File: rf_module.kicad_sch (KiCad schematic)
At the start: 32 parts, among them J10 HJ-SMA405, J9 1042240820, Q1 BC848, Q2 BC848, U4 SIM800C

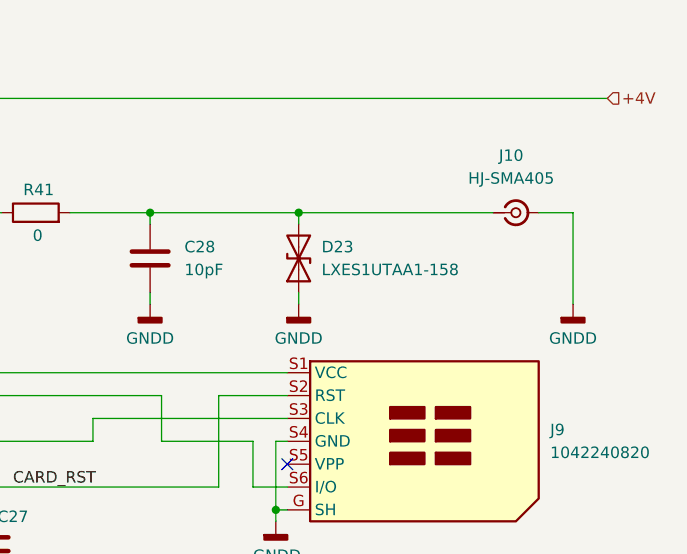
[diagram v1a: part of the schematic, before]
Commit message: Inductance was replaced
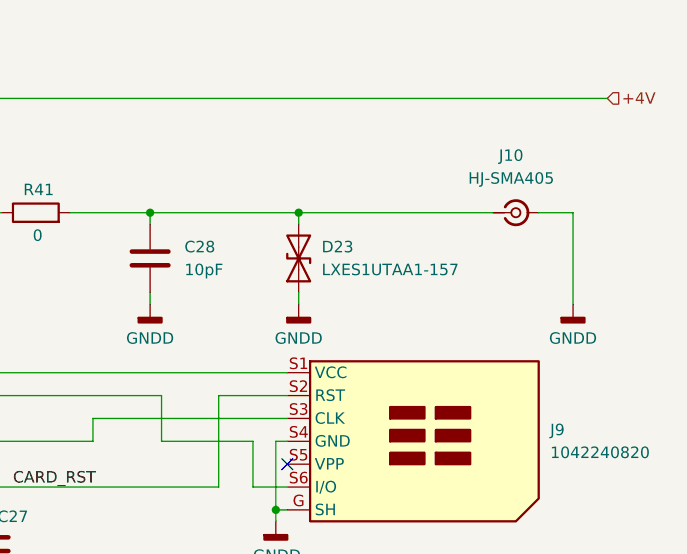
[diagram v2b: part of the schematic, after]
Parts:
- D23: value LXES1UTAA1-158 -> LXES1UTAA1-157
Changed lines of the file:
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@@
 			)
 		)
-		(property "Value" "LXES1UTAA1-158"
+		(property "Value" "LXES1UTAA1-157"
 			(at 229.87 64.7699 90)
 			(effects
